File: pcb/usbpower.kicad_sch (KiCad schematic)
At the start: 21 parts, among them J1 USB_C_Receptacle_USB2.0_14P, J2 Battery, SW3 POWER, U2 MCP1700x-330xxTT, U3 USBLC6-2SC6, U6 TP4056-42-ESOP8

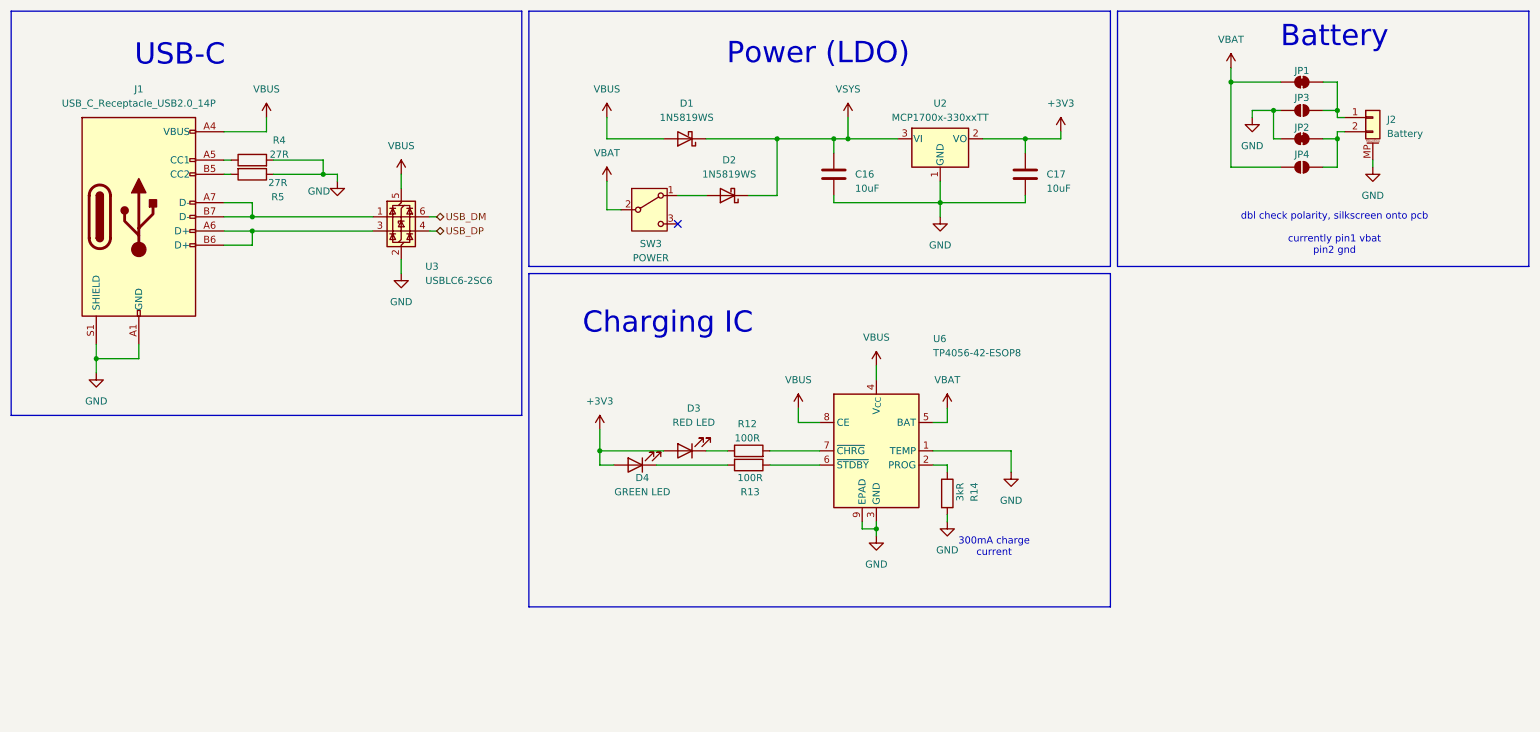
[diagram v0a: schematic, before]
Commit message: nfc tuning, new charger IC
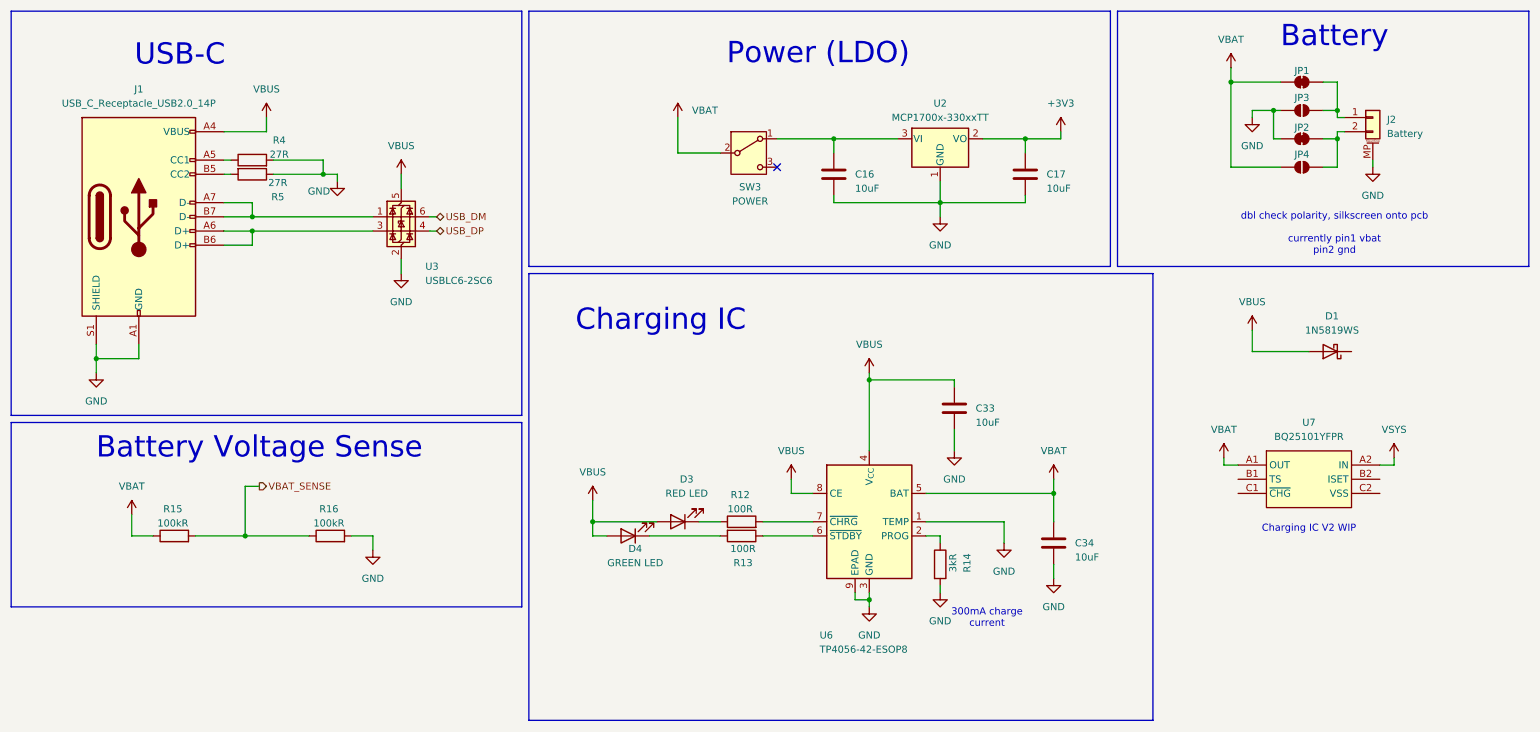
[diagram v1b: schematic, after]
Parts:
- removed D2: 1N5819WS, Diode_SMD:D_SOD-323, symbol Diode:1N5819WS
- added C33, C34: 10uF, symbol Device:C
- added R15, R16: 100kR, symbol Device:R
- added U7: BQ25101YFPR, easyeda2kicad:DSBGA-6_L0.9-W1.6-R2-C3-P0.40-BL, symbol easyeda:BQ25101YFPR
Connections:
- net +3V3: no longer D3.2 (A), D4.2 (A)
- net GND: now also C33.2, C34.2, R16.2
- net VBAT: now also C34.1, R15.1, U7.A1 (OUT)
- net VBUS: now also D3.2 (A), D4.2 (A), C33.1
- net VSYS: now also U7.A2 (IN); no longer C16.1, D1.1 (K), U2.3 (VI)
- net at SW3.1 (A): now also C16.1, U2.3 (VI)
- new net VBAT_SENSE: R15.2, R16.1
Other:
- note added: "Battery Voltage Sense"
- note added: "Charging IC V2 WIP"
- moved on the sheet: D1, D3, D4, R12, R13, R14, SW3, U6
